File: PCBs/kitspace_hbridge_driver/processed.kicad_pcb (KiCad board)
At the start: 2 copper layers, 71 x 45.5 mm, 37 parts, among them J1 Conn_01x02, J2 Conn_01x02, J3 Conn_01x04, J6 Conn_01x02, Q1 IRF9Z34NPBF, Q2 IRF9Z34NPBF, Q3 IRFZ24NPBF, Q4 IRFZ24NPBF, U1 TC4420CPA, U2 TC4420CPA

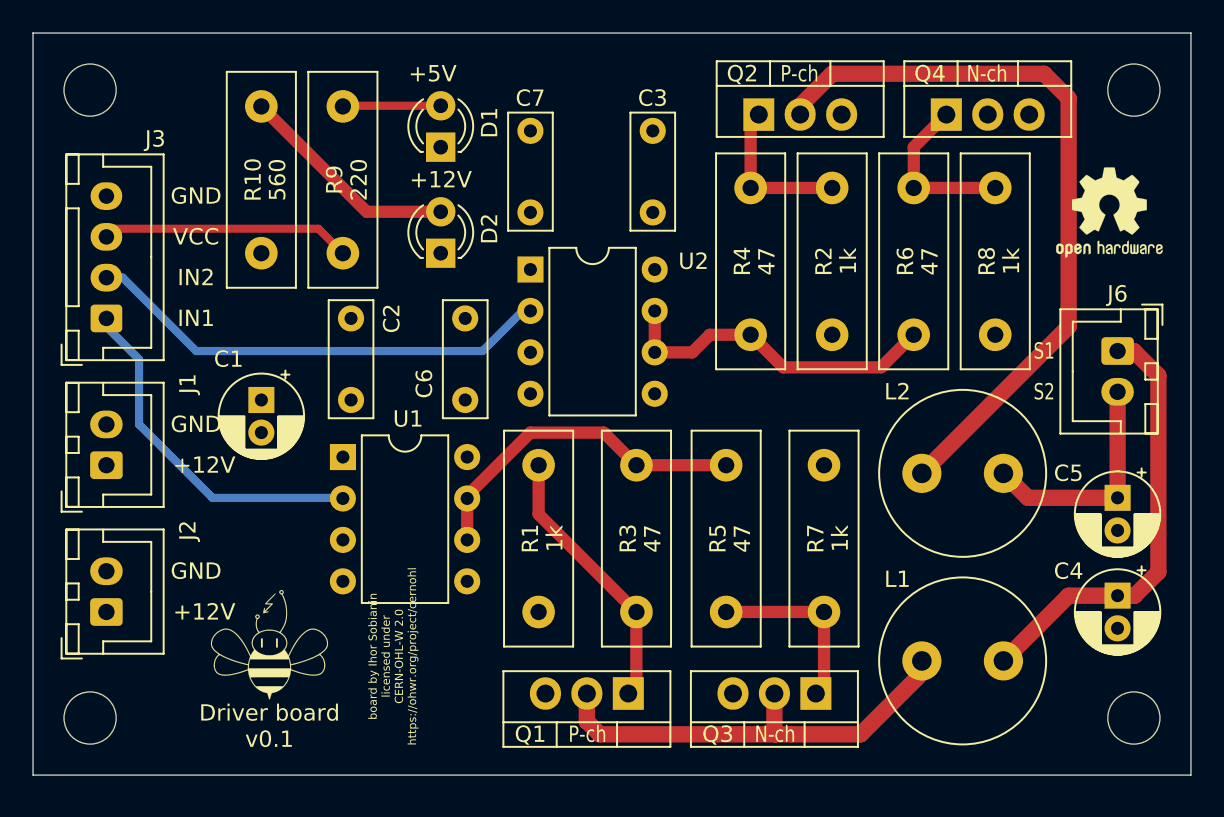
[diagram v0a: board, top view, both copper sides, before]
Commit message: recheck all circuits and clean up fill zone by rerouting the nets using freerouting and manually
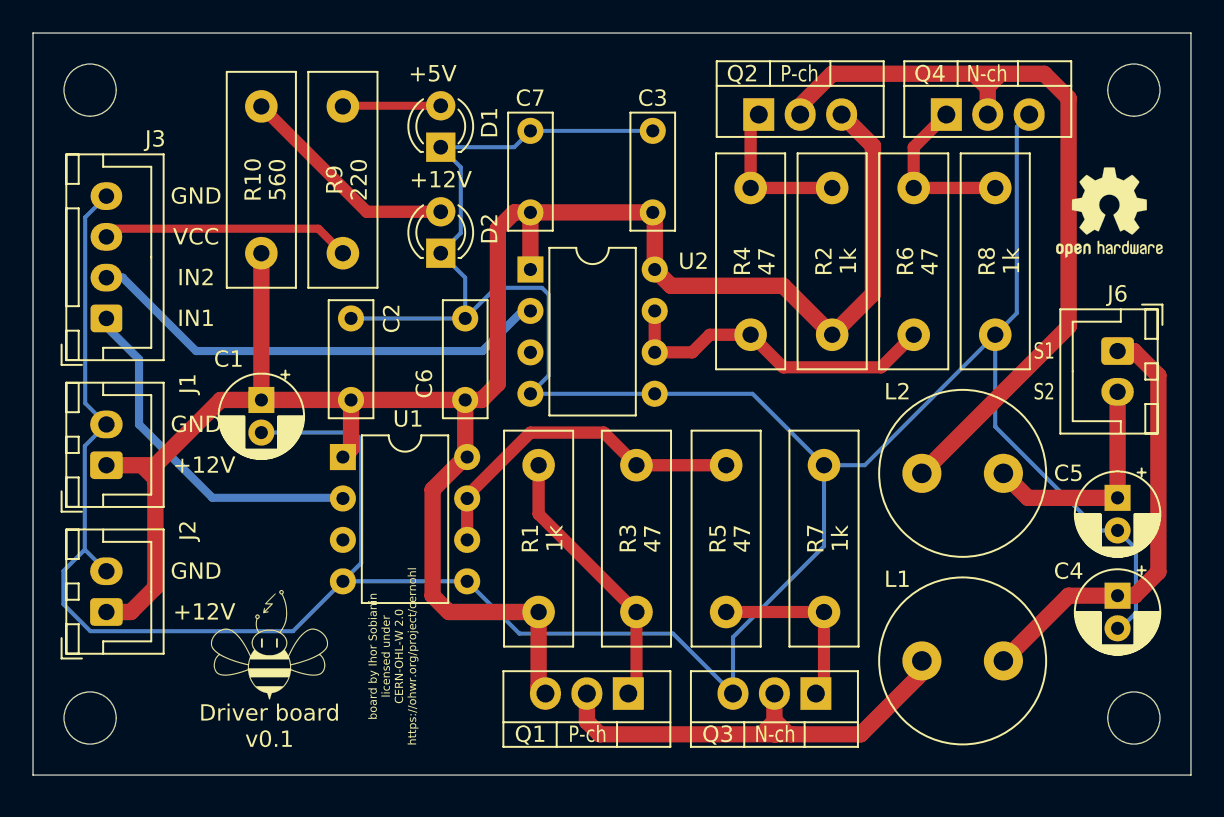
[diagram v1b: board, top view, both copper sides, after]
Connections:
- C1 pad 1: (no net) -> +12V
- C1 pad 2: (no net) -> GND
- C2 pad 1: (no net) -> +12V
- C2 pad 2: (no net) -> GND
- C3 pad 1: (no net) -> +12V
- C3 pad 2: (no net) -> GND
- C4 pad 2: (no net) -> GND
- C5 pad 2: (no net) -> GND
- C6 pad 1: (no net) -> +12V
- C6 pad 2: (no net) -> GND
- C7 pad 1: (no net) -> +12V
- C7 pad 2: (no net) -> GND
- D1 pad 1: (no net) -> GND
- D2 pad 1: (no net) -> GND
- J1 pad 1: (no net) -> +12V
- J1 pad 2: (no net) -> GND
- J2 pad 1: (no net) -> +12V
- J2 pad 2: (no net) -> GND
- J3 pad 4: (no net) -> GND
- Q1 pad 3: (no net) -> +12V
- Q2 pad 3: (no net) -> +12V
- Q3 pad 3: (no net) -> GND
- Q4 pad 2: (no net) -> Net-(L2-Pad1)
- Q4 pad 3: (no net) -> GND
- R1 pad 2: (no net) -> +12V
- R10 pad 1: (no net) -> +12V
- R2 pad 2: (no net) -> +12V
- R7 pad 1: (no net) -> GND
- R8 pad 1: (no net) -> GND
- U1 pad 1: (no net) -> +12V
- U1 pad 3: (no net) -> Net-(U1-Pad3)
- U1 pad 4: (no net) -> GND
- U1 pad 5: (no net) -> GND
- U1 pad 8: (no net) -> +12V
- U2 pad 1: (no net) -> +12V
- U2 pad 3: (no net) -> Net-(U2-Pad3)
- U2 pad 4: (no net) -> GND
- U2 pad 5: (no net) -> GND
- U2 pad 8: (no net) -> +12V
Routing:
- net GND: track 0.00 -> 222.6 mm
- net +12V: track 0.00 -> 130.8 mm
- net Net-(L2-Pad1): track 45.2 -> 50.1 mm
- net Net-(L1-Pad1): track 27.4 -> 30.6 mm

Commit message: clean psbc that are missed before
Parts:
- removed the REF** at (127.5, 74.5)
- removed the REF** at (191.5, 74.5)
- added REF**_2: MountingHole_3.2mm_M3_DIN965, MountingHole:MountingHole_3.2mm_M3_DIN965, F.Cu at (191.5, 74.5)
- added REF**_3: MountingHole_3.2mm_M3_DIN965, MountingHole:MountingHole_3.2mm_M3_DIN965, F.Cu at (127.5, 74.5)
- renumbered REF** to REF**_4, REF** to REF**_5
